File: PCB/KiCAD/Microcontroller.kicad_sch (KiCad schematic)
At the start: 20 parts, among them J6 Conn_01x06, U8 RP2040, Y1 Crystal_GND24

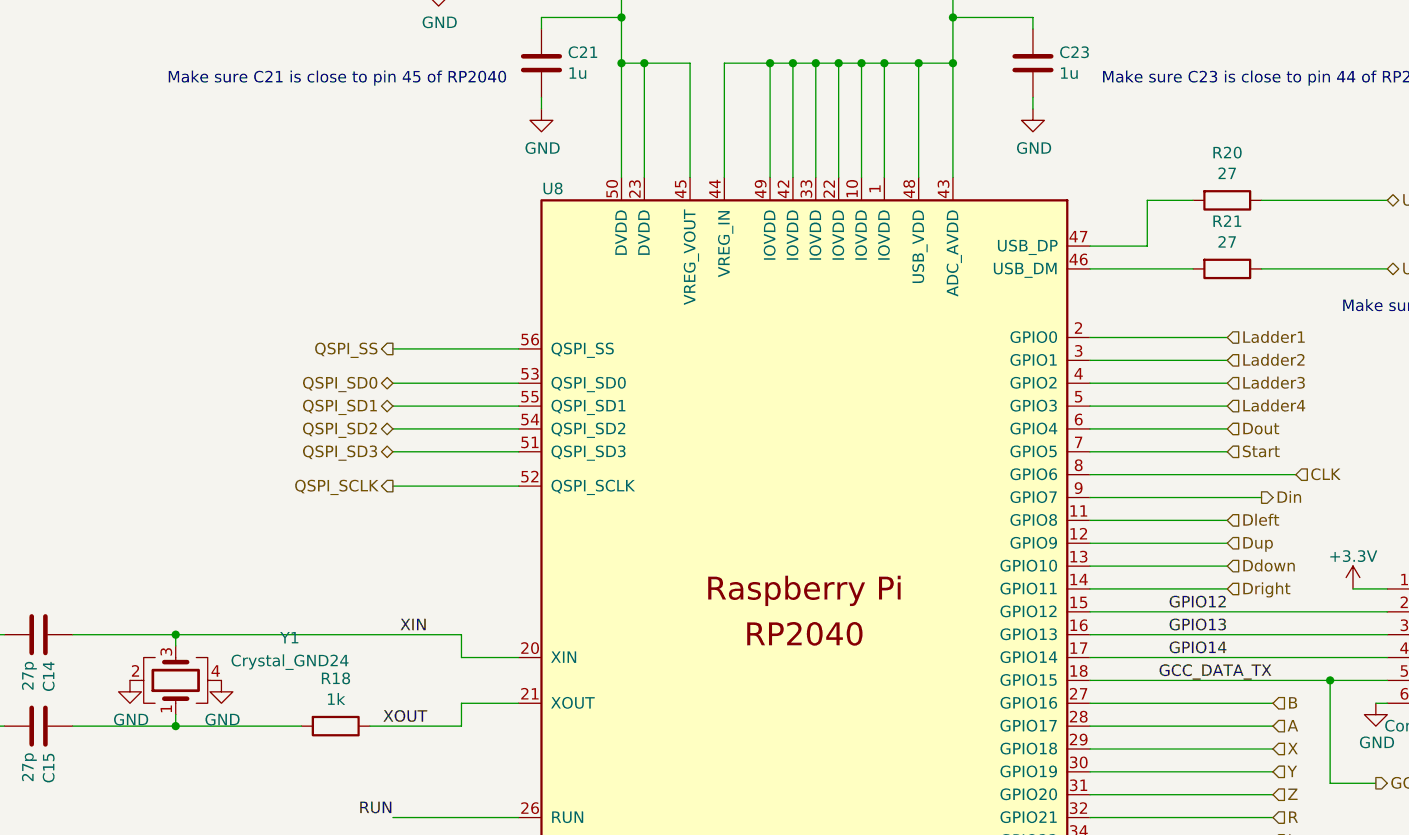
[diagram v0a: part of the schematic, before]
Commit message: Assembly and fab upload
Upload schematic pdf and bom csv and ibom html docs
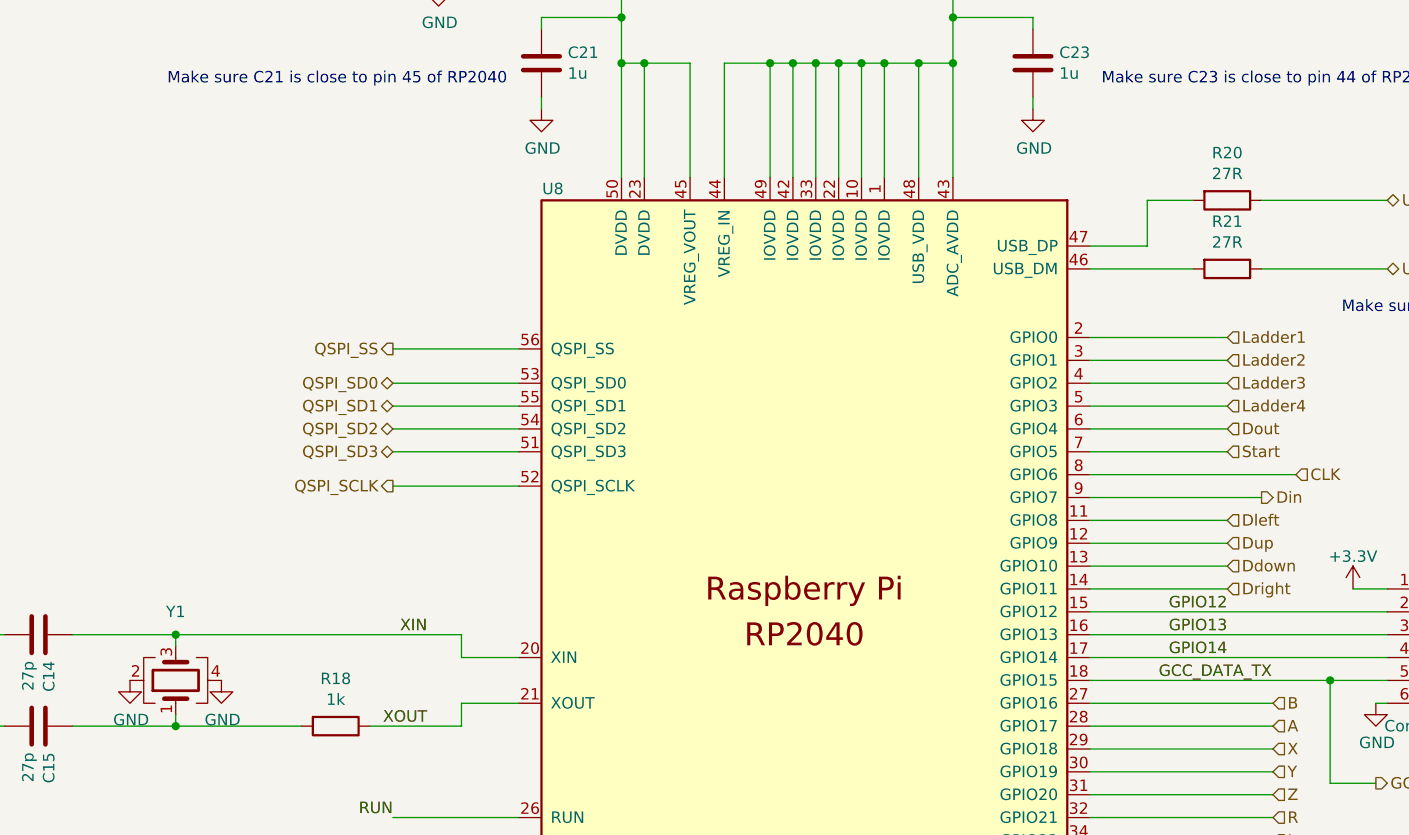
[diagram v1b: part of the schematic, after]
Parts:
- C14, C15: MPN (none) -> 0402YA270JAT2A; Manufacturer (none) -> KYOCERA AVX; Package (none) -> 0402; VARIANT (none) -> NoVar
- C19, C20, C22, C24, C25, C26, C27, C28, C29, C31: MPN (none) -> CL05B104KA5NNNC; Manufacturer (none) -> Samsung Electro-Mechanics; Package (none) -> 0402; VARIANT (none) -> NoVar
- C21, C23: MPN (none) -> GRM155Z71A105KE01J; Manufacturer (none) -> Murata Electronics; Package (none) -> 0402; VARIANT (none) -> NoVar
- J6: DNP (none) -> DNP; Package (none) -> Through-Hole; VARIANT (none) -> NoVar
- R18: MPN (none) -> RMCF0402FT1K00; Manufacturer (none) -> Stackpole Electronics Inc; Package (none) -> 0402; VARIANT (none) -> NoVar
- R20, R21: value 27 -> 27R; MPN (none) -> RC0402FR-0727RL; Manufacturer (none) -> YAGEO; Package (none) -> 0402; VARIANT (none) -> NoVar
- U8: MPN (none) -> SC0914(13); Manufacturer (none) -> Raspberry Pi; Package (none) -> 56-QFN; VARIANT (none) -> NoVar
- Y1: LCSC (none) -> C403945; MPN (none) -> RH100-12.000-18-2020-EXT-TR; Manufacturer (none) -> Raltron Electronics; Package (none) -> SMD-3225; VARIANT (none) -> NoVar
